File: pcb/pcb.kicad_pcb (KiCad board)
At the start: 2 copper layers, 115.2 x 76.8 mm, 62 parts, among them J1 TYPE-C-31-M-12, J2 AudioJack4, J3 AudioJack4, SW1 SW_Push, SW10 SW_Push, SW11 SW_Push, SW12 SW_Push, SW13 SW_Push, SW14 SW_Push, SW15 SW_Push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

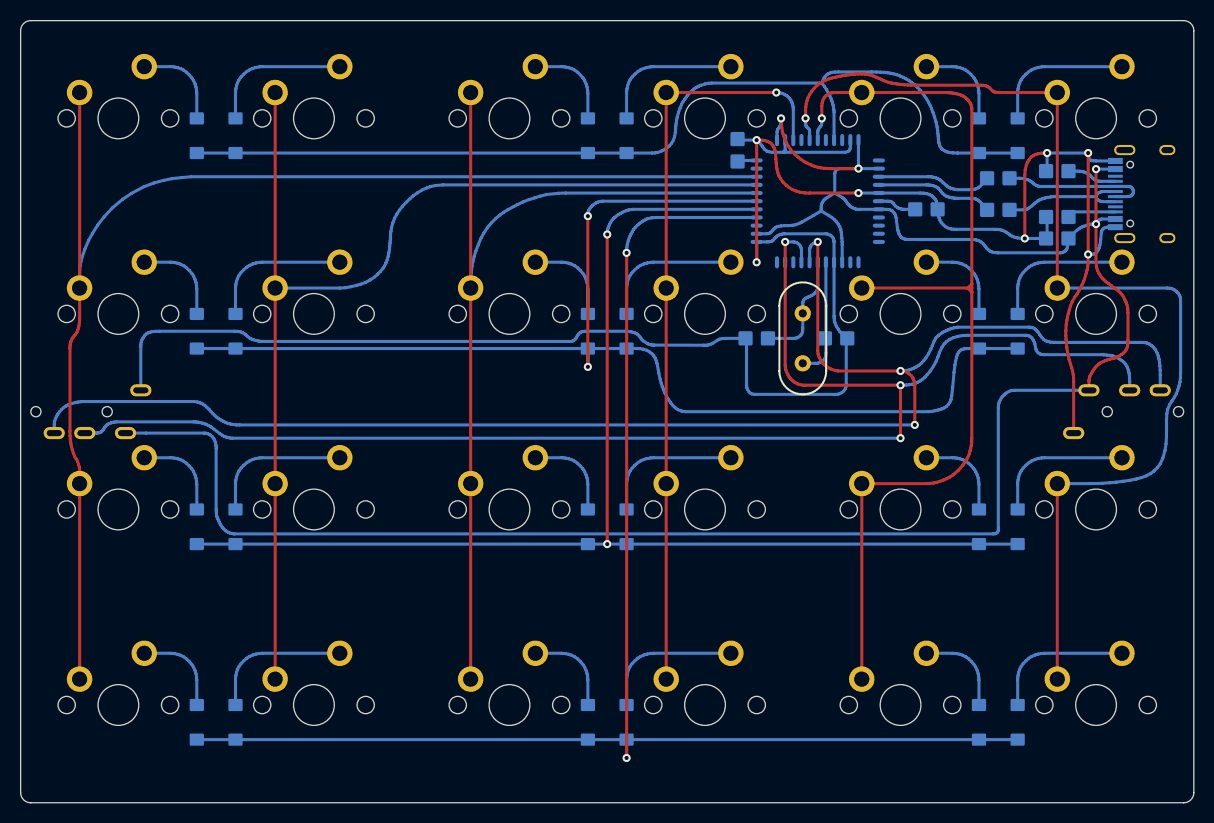
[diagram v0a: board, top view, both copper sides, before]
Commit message: routing beautify & product number
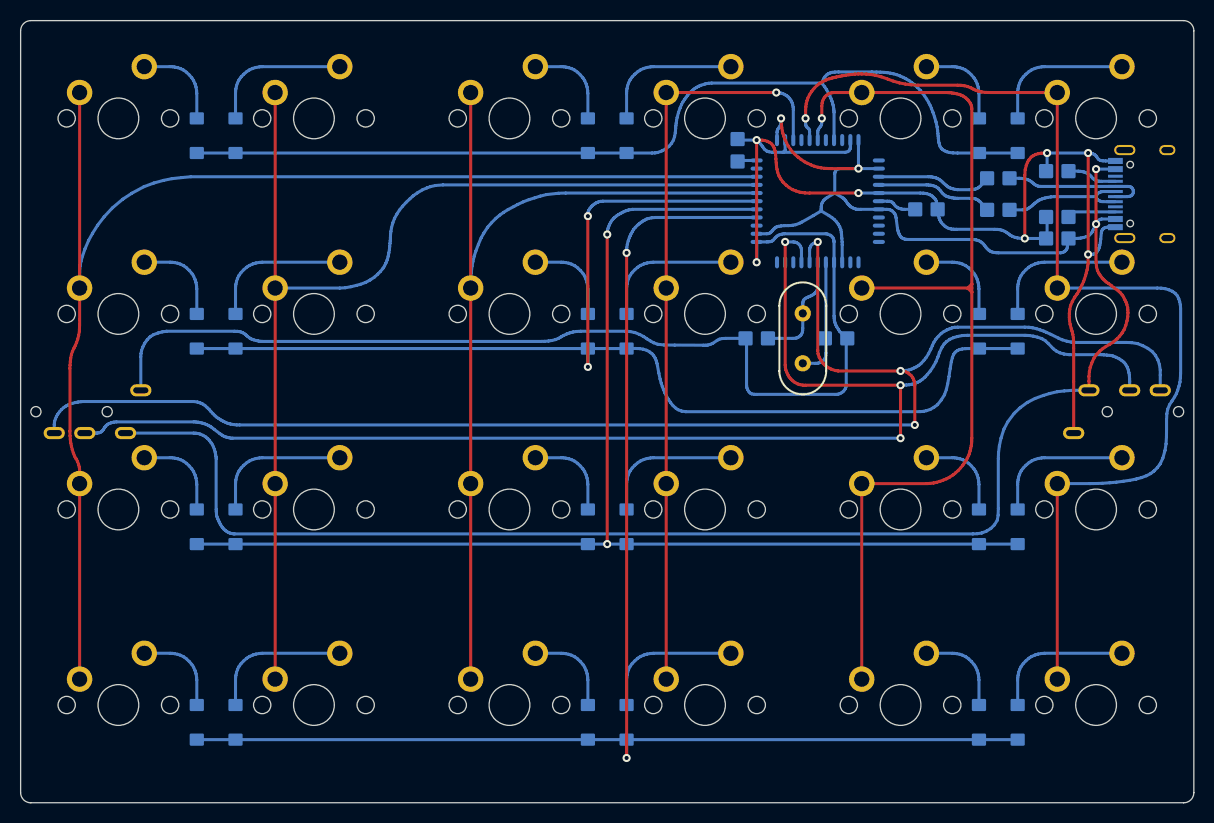
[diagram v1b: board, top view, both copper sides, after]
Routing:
- net VCC: track 212.8 -> 209.2 mm
- net GND: track 219.8 -> 218.6 mm
- net SCL: track 147.5 -> 146.8 mm
- net SDA: track 142.4 -> 141.8 mm
- net R1: track 123.0 -> 122.5 mm
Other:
- board text added: "kakudo 4421"

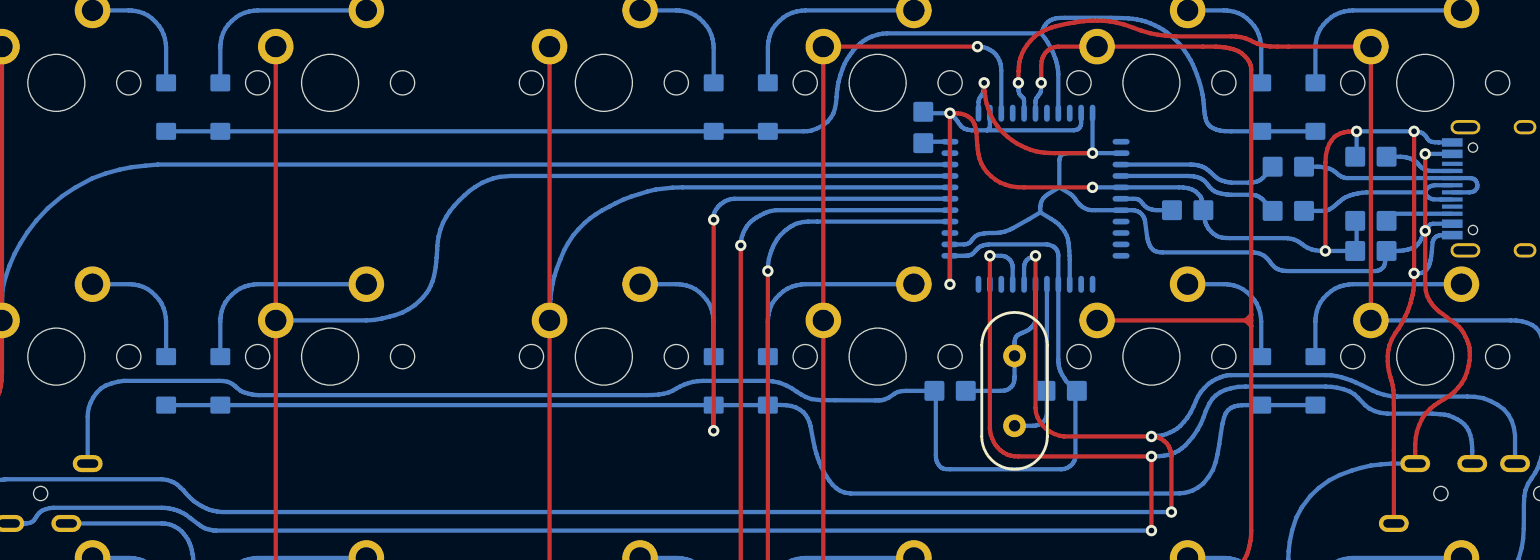
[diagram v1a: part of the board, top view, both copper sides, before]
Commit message: smd 2012 beautify
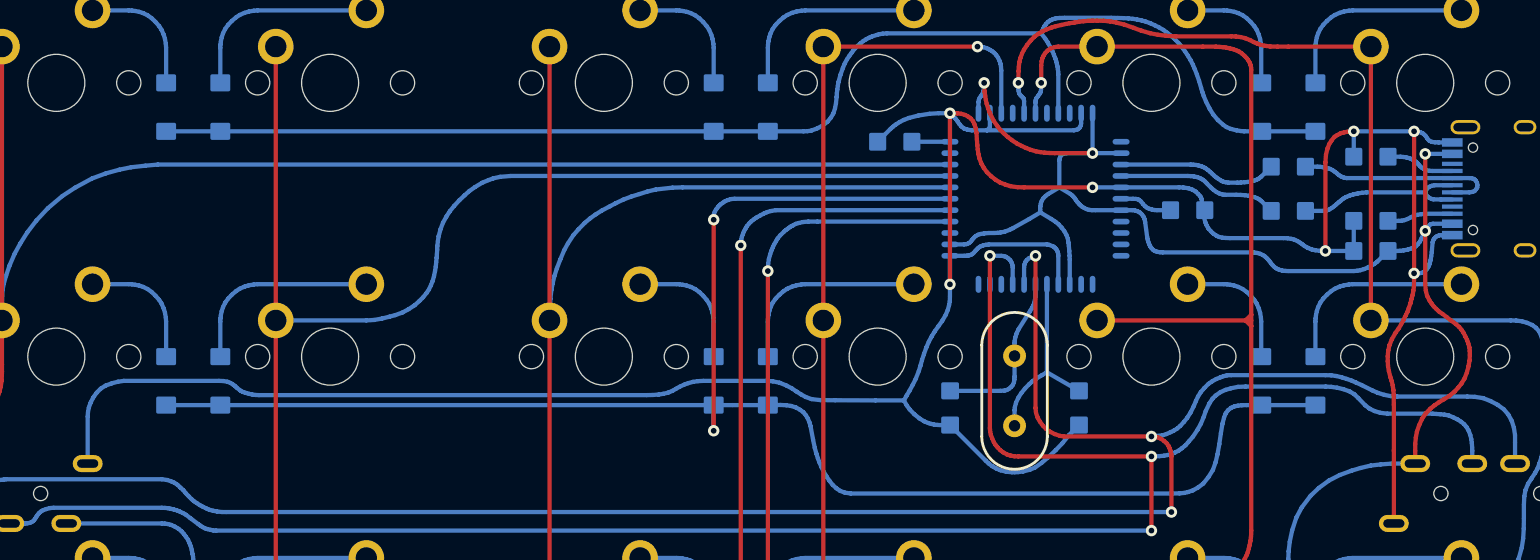
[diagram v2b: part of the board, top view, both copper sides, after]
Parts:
- moved R1 2.24 mm to (68.4, 13.7), turned to 0 degrees
- moved C2 1.73 mm to (81.3, 32.4), turned to 270 degrees
- moved C1 1.20 mm to (72.3, 32.4), turned to 270 degrees
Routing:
- net GND: track 218.6 -> 216.5 mm
- net Net-(C2-Pad1): track 11.8 -> 13.5 mm
- net Net-(R1-Pad2): track 1.87 -> 2.67 mm
- net VCC: track 209.2 -> 208.5 mm
- net R0: track 95.9 -> 95.3 mm
- net Net-(C1-Pad1): track 11.3 -> 12.0 mm

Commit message: + reset button
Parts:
- added R6: 10k, SMD:2012M, B.Cu at (88.9, 20.9)
- added RST1: SW_Push, Button_Switch_SMD:SW_SPST_TL3342, B.Cu at (96.0, 38.4)
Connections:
- U1 pad 13: (no net) -> RESET
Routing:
- net RESET: track 0.00 -> 35.4 mm, vias 0 -> 2
- net GND: track 216.5 -> 228.1 mm
- net VCC: track 208.5 -> 207.5 mm
- net Net-(D18-Pad2): track 14.2 -> 13.4 mm
